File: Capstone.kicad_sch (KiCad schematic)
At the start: 3 parts, among them J2 Conn_01x08_Socket, U1 ESP32-C3-WROOM-02, U3 74LS151

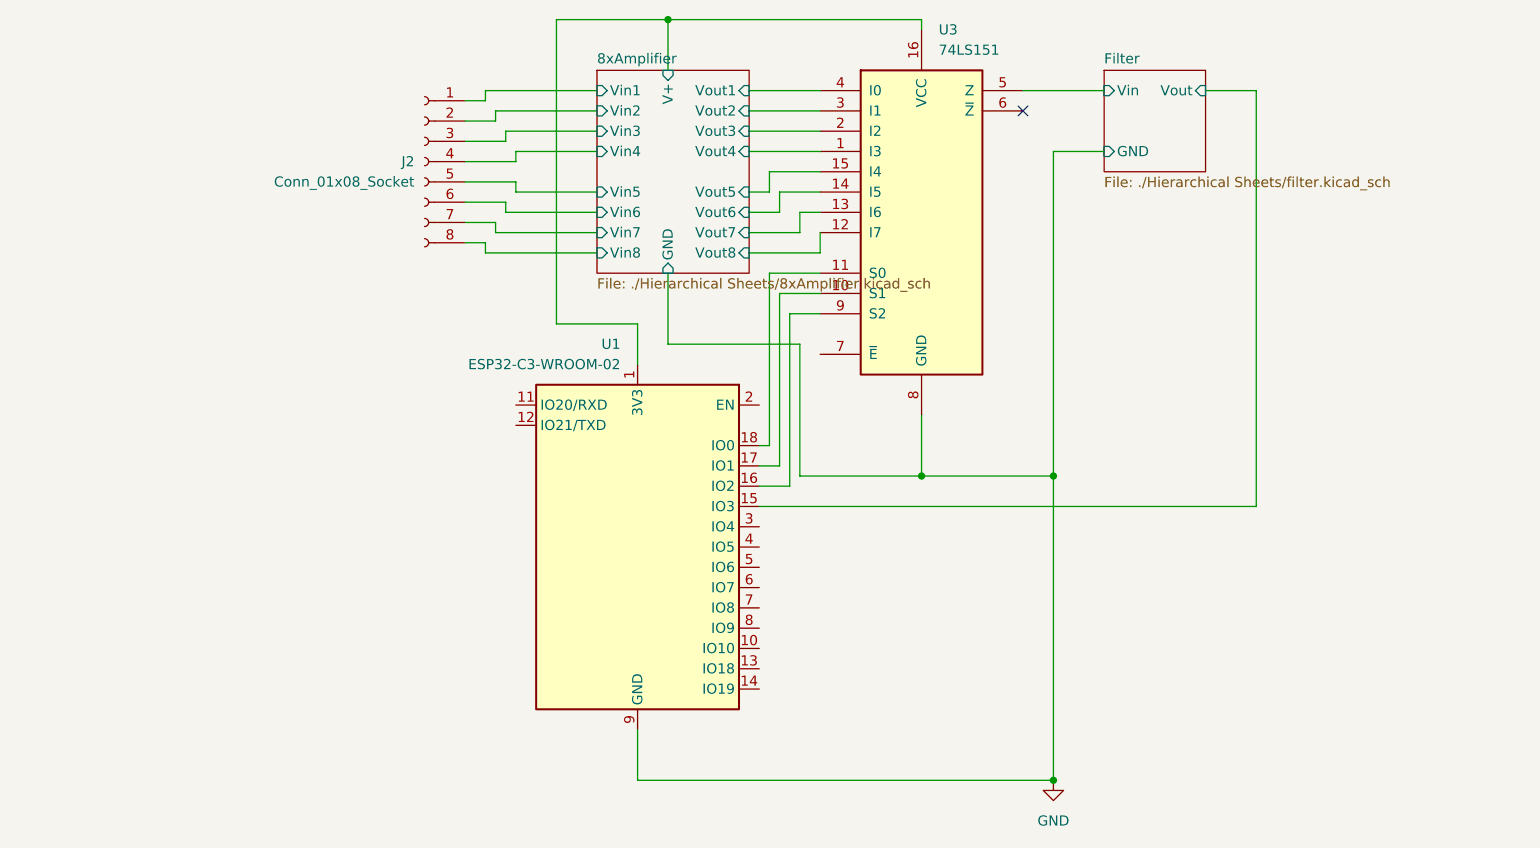
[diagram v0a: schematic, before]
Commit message: SN74HC161DR symbol update
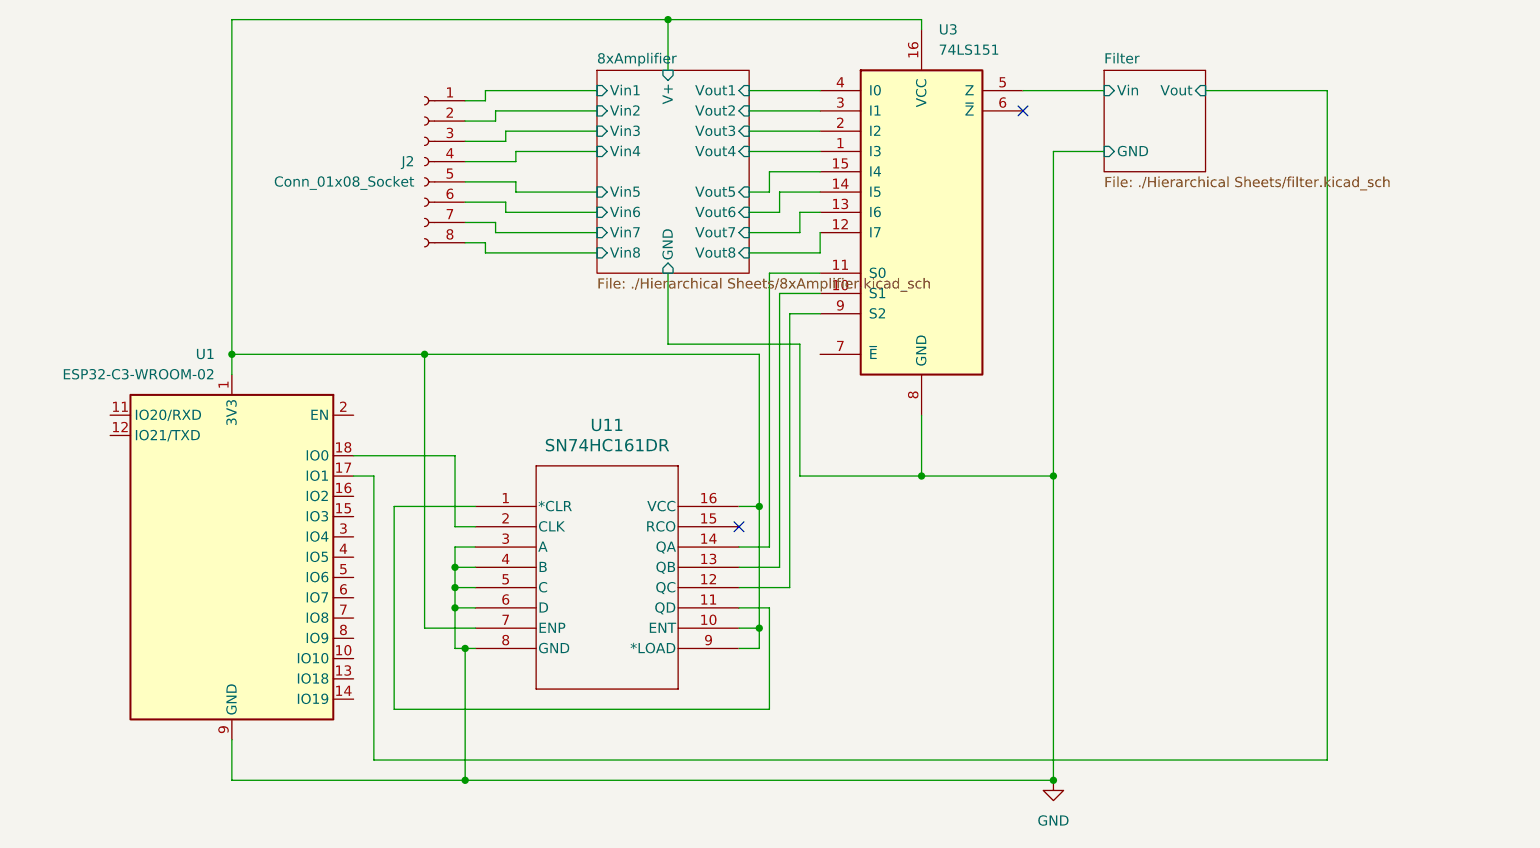
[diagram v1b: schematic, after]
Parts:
- added U11: SN74HC161DR, D16, symbol Capstone:SN74HC161DR
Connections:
- net 8xAmplifier/V+: now also U11.10 (ENT), U11.16 (VCC), U11.7 (ENP), U11.9 (*LOAD)
- net Filter/Vout: now also U1.17 (IO1); no longer U1.15 (IO3)
- net GND: now also U11.3 (A), U11.4 (B), U11.5 (C), U11.6 (D), U11.8 (GND)
- net at U3.10 (S1): now also U11.13 (QB); no longer U1.17 (IO1)
- net at U3.11 (S0): now also U11.14 (QA); no longer U1.18 (IO0)
- net at U3.9 (S2): now also U11.12 (QC); no longer U1.16 (IO2)
- new net: U1.18 (IO0), U11.2 (CLK)
- new net: U11.1 (*CLR), U11.11 (QD)
- no-connect marks 1 -> 2
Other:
- moved on the sheet: U1
